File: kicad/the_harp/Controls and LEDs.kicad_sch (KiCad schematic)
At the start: 39 parts, among them SW101 100-DP6, SW102 100-DP6, SW103 100-DP6

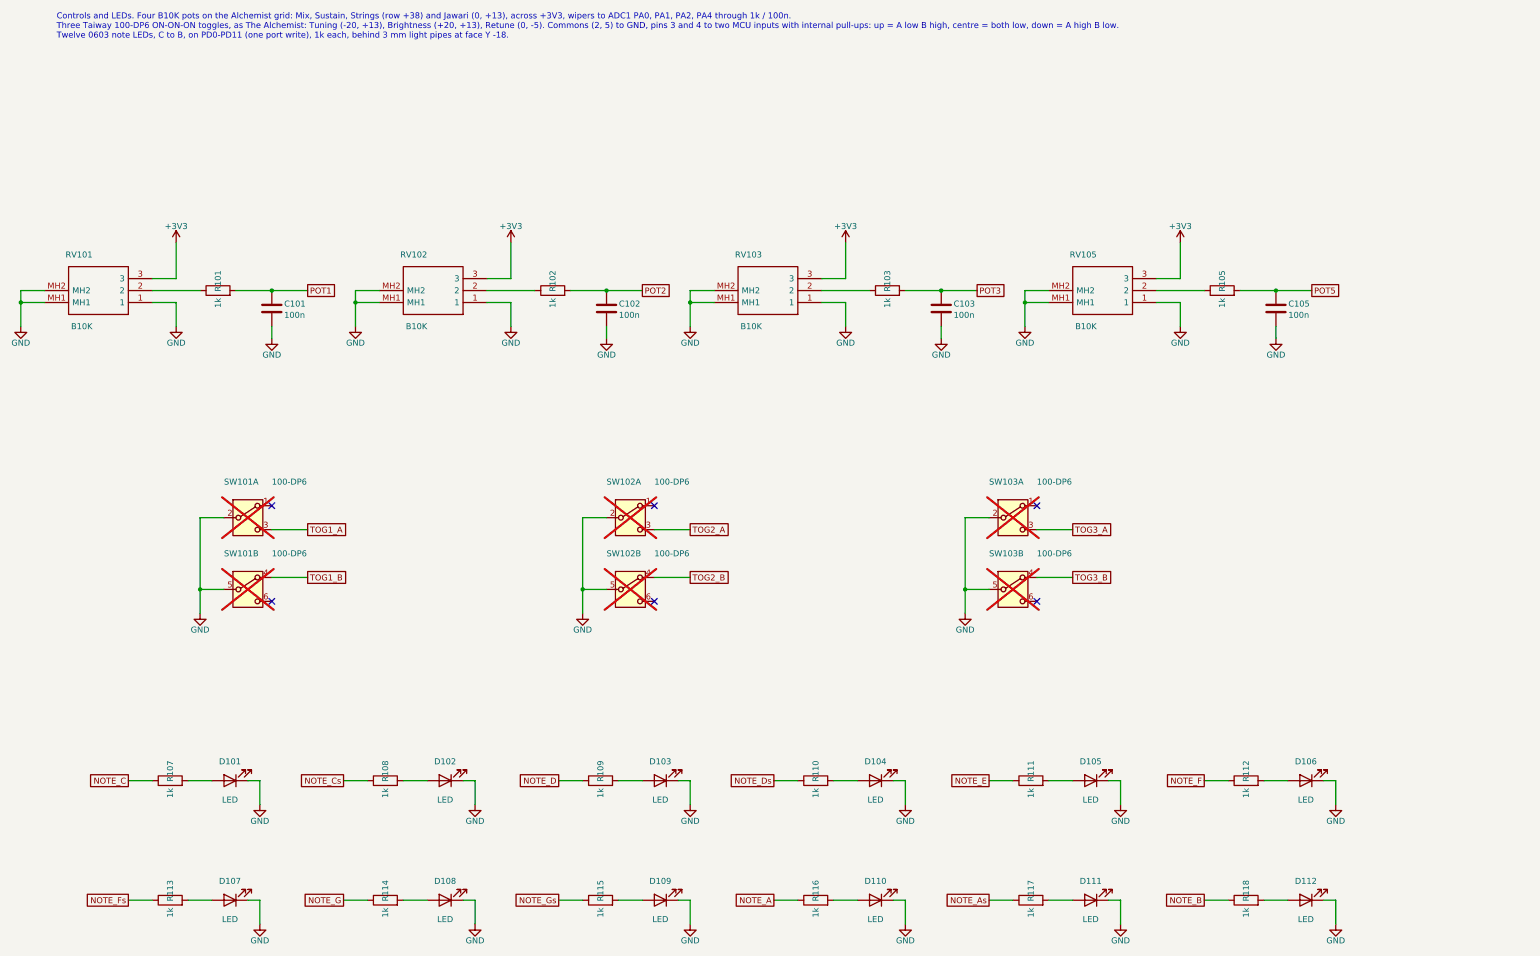
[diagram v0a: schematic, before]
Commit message: Stereo single-ended input and an OLED display
IN becomes a TRS jack (tip left, ring right) with a second OPA2365 buffer and
THS4522 channel B into the AK4621EF's AINR; the codec inputs are no longer
parked. A mono plug is detected by the right channel reading silence. The
twelve note LEDs and R107-R118 give way to a 0.91 in I2C OLED connector (J408,
PB6/PB7) with 4.7k pull-ups. Schematic regenerated (190 parts, netlist OK on
all sheets); design brief, PCB plan, firmware requirements and the design
report updated. The PCB still carries the old LED footprints until Update PCB
from Schematic is run in KiCad.

Co-Authored-By: Claude Sonnet 5.5 <noreply@anthropic.com>
Claude-Session: https://claude.ai/code/session_016hDejPHPgG8auBLMyByYZK
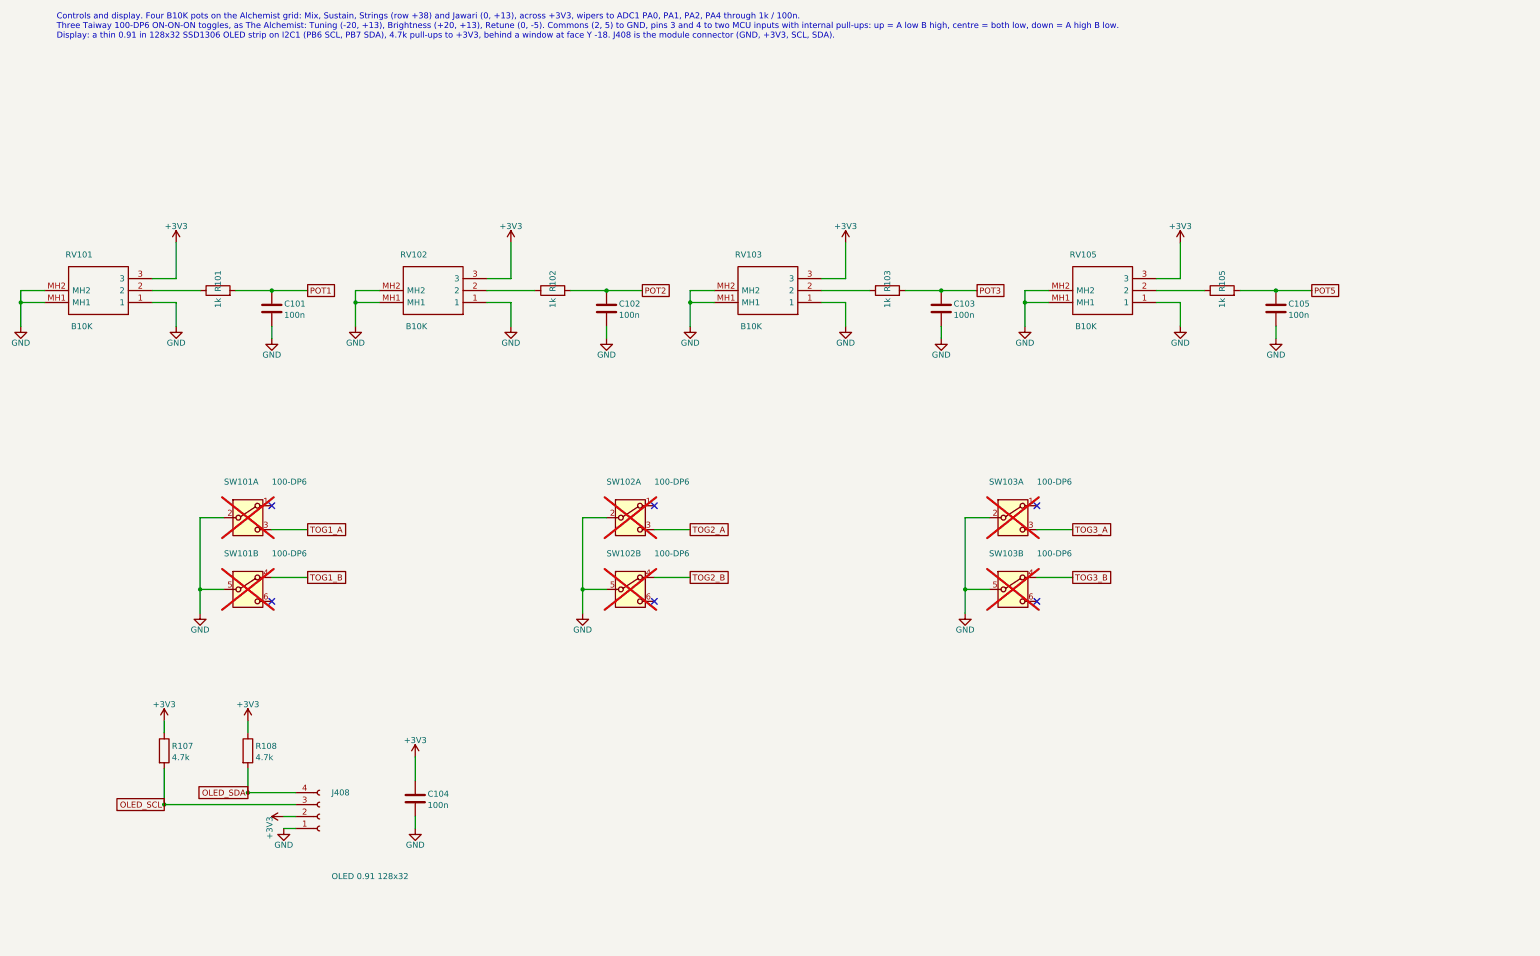
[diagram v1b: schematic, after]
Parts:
- removed D101, D102, D103, D104, D105, D106, D107, D108, D109, D110, D111, D112: LED, LED_SMD:LED_0603_1608Metric, symbol Device:LED
- removed R109, R110, R111, R112, R113, R114, R115, R116, R117, R118: 1k, Resistor_SMD:R_0603_1608Metric, symbol Device:R
- added C104: 100n, Capacitor_SMD:C_0603_1608Metric, symbol Device:C
- added J408: OLED 0.91 128x32, Connector_JST:JST_SH_SM04B-SRSS-TB_1x04-1MP_P1.00mm_Horizontal, symbol Connector:Conn_01x04_Socket
- R107, R108: value 1k -> 4.7k
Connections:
- net NOTE_C is gone; now on net +3V3: R107.1
- net NOTE_Cs is gone; now on net +3V3: R108.1
- net +3V3: now also C104.1, J408.2 (Pin_2)
- net GND: now also C104.2, J408.1 (Pin_1)
- net OLED_SDA: now reaches R108.2
- net OLED_SDA: now also J408.4 (Pin_4)
- net OLED_SCL: now reaches R107.2
- net OLED_SCL: now also J408.3 (Pin_3)
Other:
- note added: "Controls and display. Four B10K pots on the Alchemist grid: Mix, Sustain, Strings (row +38) and Jawari (0, +13), across +3V3, wipers to ADC1 PA0, PA1, PA2, PA4 through 1k / 100n. Three Taiway 100-DP6 ON-ON-ON toggles, as The Alchemist: Tuning (-20, +13), Brightness (+20, +13), Retune (0, -5). Commons (2, 5) to GND, pins 3 and 4 to two MCU inputs with internal pull-ups: up = A low B high, centre =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"
- note removed: "Controls and LEDs. Four B10K pots on the Alchemist grid: Mix, Sustain, Strings (row +38) and Jawari (0, +13), across +3V3, wipers to ADC1 PA0, PA1, PA2, PA4 through 1k / 100n. Three Taiway 100-DP6 ON-ON-ON toggles, as The Alchemist: Tuning (-20, +13), Brightness (+20, +13), Retune (0, -5). Commons (2, 5) to GND, pins 3 and 4 to two MCU inputs with internal pull-ups: up = A low B high, centre = bo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"
- moved on the sheet: R107, R108
